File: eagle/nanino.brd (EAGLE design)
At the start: 68.6 x 53.3 mm, 19 parts, among them IC1 ATMEGA328P-20, Q1 16MHz

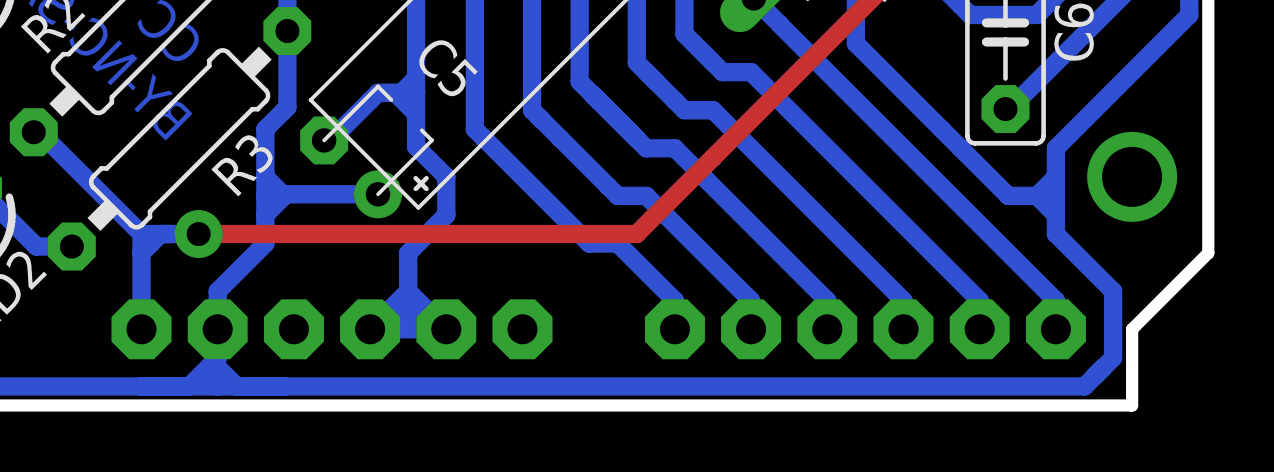
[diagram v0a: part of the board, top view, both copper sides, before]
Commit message: Power was connected to 3.3V Pin, not to 5V
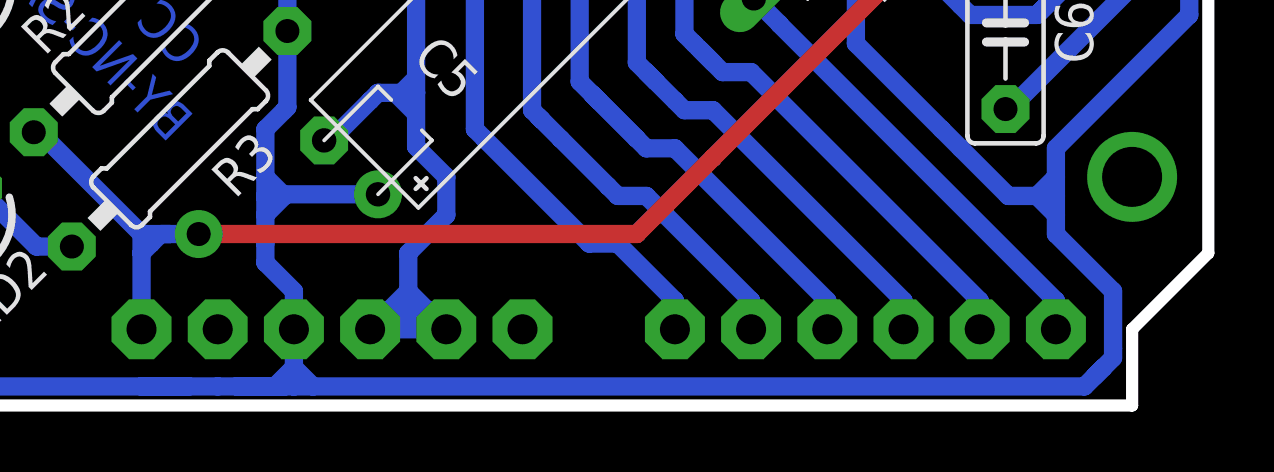
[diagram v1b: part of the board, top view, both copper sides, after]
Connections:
- net VCC: now also PWR_.3; no longer PWR_.2
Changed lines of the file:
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@@
 <layers>
 <layer number="1" name="Top" color="4" fill="1" visible="yes" active="yes"/>
-<layer number="16" name="Bottom" color="1" fill="1" visible="no" active="yes"/>
+<layer number="16" name="Bottom" color="1" fill="1" visible="yes" active="yes"/>
 <layer number="17" name="Pads" color="2" fill="1" visible="yes" active="yes"/>
 <layer number="18" name="Vias" color="2" fill="1" visible="yes" active="yes"/>
@@
 <contactref element="R2" pad="2"/>
 <contactref element="FTDI_" pad="3"/>
-<contactref element="PWR_" pad="2"/>
+<contactref element="PWR_" pad="3"/>
 <contactref element="IC1" pad="7"/>
 <contactref element="IC1" pad="20"/>
@@
 <wire x1="33.02" y1="0.635" x2="25.7175" y2="0.635" width="0.6096" layer="16"/>
 <wire x1="37.465" y1="0.635" x2="37.7825" y2="0.635" width="0.6096" layer="16"/>
-<wire x1="37.7825" y1="0.635" x2="64.4525" y2="0.635" width="0.6096" layer="16"/>
+<wire x1="37.7825" y1="0.635" x2="38.1" y2="0.635" width="0.6096" layer="16"/>
+<wire x1="38.1" y1="0.635" x2="38.735" y2="0.635" width="0.6096" layer="16"/>
+<wire x1="38.735" y1="0.635" x2="64.4525" y2="0.635" width="0.6096" layer="16"/>
 <wire x1="64.4525" y1="0.635" x2="65.0875" y2="1.27" width="0.6096" layer="16"/>
 <wire x1="24.4475" y1="0.9525" x2="24.765" y2="0.635" width="0.6096" layer="16"/>
 <wire x1="24.765" y1="0.635" x2="25.7175" y2="0.635" width="0.6096" layer="16"/>
-<wire x1="35.56" y1="2.54" x2="35.56" y2="1.5875" width="0.6096" layer="16"/>
-<wire x1="35.56" y1="1.5875" x2="34.6075" y2="0.635" width="0.6096" layer="16"/>
 <wire x1="34.6075" y1="0.635" x2="33.02" y2="0.635" width="0.6096" layer="16"/>
 <wire x1="33.02" y1="0.635" x2="35.56" y2="0.635" width="0.6096" layer="16"/>
 <wire x1="35.56" y1="0.635" x2="36.195" y2="0.635" width="0.6096" layer="16"/>
-<wire x1="36.195" y1="0.635" x2="37.7825" y2="0.635" width="0.6096" layer="16"/>
-<wire x1="37.7825" y1="0.635" x2="36.195" y2="0.635" width="0.6096" layer="16"/>
-<wire x1="36.195" y1="0.635" x2="35.56" y2="1.27" width="0.6096" layer="16"/>
-<wire x1="35.56" y1="1.27" x2="35.56" y2="0.635" width="0.6096" layer="16"/>
+<wire x1="36.195" y1="0.635" x2="37.465" y2="0.635" width="0.6096" layer="16"/>
+<wire x1="37.465" y1="0.635" x2="37.7825" y2="0.635" width="0.6096" layer="16"/>
+<wire x1="37.7825" y1="0.635" x2="37.465" y2="0.635" width="0.6096" layer="16"/>
+<wire x1="37.465" y1="0.635" x2="36.195" y2="0.635" width="0.6096" layer="16"/>
 <wire x1="38.4175" y1="15.5575" x2="40.005" y2="15.5575" width="0.6096" layer="16"/>
 <wire x1="40.005" y1="15.5575" x2="40.376971875" y2="15.929471875" width="0.6096" layer="16"/>
@@
 <wire x1="37.1475" y1="7.62" x2="37.1475" y2="6.985" width="0.6096" layer="16"/>
 <wire x1="37.1475" y1="6.985" x2="37.1475" y2="6.933471875" width="0.6096" layer="16"/>
-<wire x1="35.56" y1="2.54" x2="35.56" y2="3.81" width="0.6096" layer="16"/>
-<wire x1="35.56" y1="3.81" x2="37.1475" y2="5.3975" width="0.6096" layer="16"/>
 <wire x1="37.1475" y1="5.3975" x2="37.1475" y2="6.35" width="0.6096" layer="16"/>
 <wire x1="37.1475" y1="6.35" x2="37.1475" y2="6.933471875" width="0.6096" layer="16"/>
@@
 <wire x1="63.5" y1="7.62" x2="62.865" y2="6.985" width="0.6096" layer="16"/>
 <wire x1="62.865" y1="6.985" x2="63.5" y2="6.35" width="0.6096" layer="16"/>
+<wire x1="37.1475" y1="5.3975" x2="37.1475" y2="4.7625" width="0.6096" layer="16"/>
+<wire x1="37.1475" y1="4.7625" x2="38.1" y2="3.81" width="0.6096" layer="16"/>
+<wire x1="38.1" y1="3.81" x2="38.1" y2="2.54" width="0.6096" layer="16"/>
+<wire x1="38.1" y1="2.54" x2="38.1" y2="1.27" width="0.6096" layer="16"/>
+<wire x1="38.1" y1="1.27" x2="38.1" y2="0.635" width="0.6096" layer="16"/>
+<wire x1="38.1" y1="1.27" x2="37.465" y2="0.635" width="0.6096" layer="16"/>
+<wire x1="38.1" y1="1.27" x2="38.735" y2="0.635" width="0.6096" layer="16"/>
 </signal>
 <signal name="N$34">
@@
 </signal>
 </signals>
-<errors>
-</errors>
 </board>
 </drawing>

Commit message: 5V power was connected to 3.3V Pin
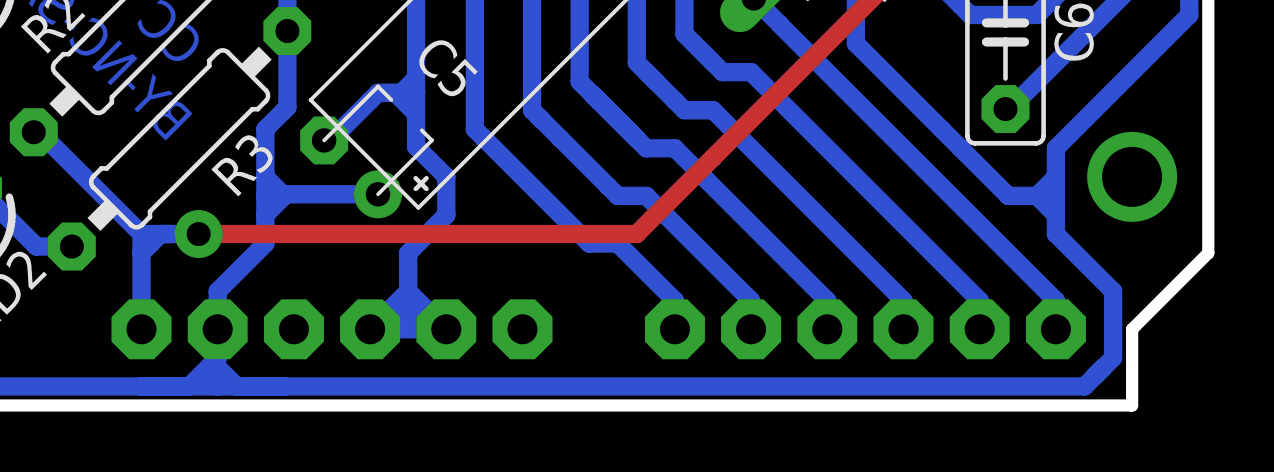
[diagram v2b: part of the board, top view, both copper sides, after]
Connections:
- net VCC: now also PWR_.2; no longer PWR_.3
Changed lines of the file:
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@@
 <layers>
 <layer number="1" name="Top" color="4" fill="1" visible="yes" active="yes"/>
-<layer number="16" name="Bottom" color="1" fill="1" visible="yes" active="yes"/>
+<layer number="16" name="Bottom" color="1" fill="1" visible="no" active="yes"/>
 <layer number="17" name="Pads" color="2" fill="1" visible="yes" active="yes"/>
 <layer number="18" name="Vias" color="2" fill="1" visible="yes" active="yes"/>
@@
 <contactref element="R2" pad="2"/>
 <contactref element="FTDI_" pad="3"/>
-<contactref element="PWR_" pad="3"/>
+<contactref element="PWR_" pad="2"/>
 <contactref element="IC1" pad="7"/>
 <contactref element="IC1" pad="20"/>
@@
 <wire x1="33.02" y1="0.635" x2="25.7175" y2="0.635" width="0.6096" layer="16"/>
 <wire x1="37.465" y1="0.635" x2="37.7825" y2="0.635" width="0.6096" layer="16"/>
-<wire x1="37.7825" y1="0.635" x2="38.1" y2="0.635" width="0.6096" layer="16"/>
-<wire x1="38.1" y1="0.635" x2="38.735" y2="0.635" width="0.6096" layer="16"/>
-<wire x1="38.735" y1="0.635" x2="64.4525" y2="0.635" width="0.6096" layer="16"/>
+<wire x1="37.7825" y1="0.635" x2="64.4525" y2="0.635" width="0.6096" layer="16"/>
 <wire x1="64.4525" y1="0.635" x2="65.0875" y2="1.27" width="0.6096" layer="16"/>
 <wire x1="24.4475" y1="0.9525" x2="24.765" y2="0.635" width="0.6096" layer="16"/>
 <wire x1="24.765" y1="0.635" x2="25.7175" y2="0.635" width="0.6096" layer="16"/>
+<wire x1="35.56" y1="2.54" x2="35.56" y2="1.5875" width="0.6096" layer="16"/>
+<wire x1="35.56" y1="1.5875" x2="34.6075" y2="0.635" width="0.6096" layer="16"/>
 <wire x1="34.6075" y1="0.635" x2="33.02" y2="0.635" width="0.6096" layer="16"/>
 <wire x1="33.02" y1="0.635" x2="35.56" y2="0.635" width="0.6096" layer="16"/>
 <wire x1="35.56" y1="0.635" x2="36.195" y2="0.635" width="0.6096" layer="16"/>
-<wire x1="36.195" y1="0.635" x2="37.465" y2="0.635" width="0.6096" layer="16"/>
-<wire x1="37.465" y1="0.635" x2="37.7825" y2="0.635" width="0.6096" layer="16"/>
-<wire x1="37.7825" y1="0.635" x2="37.465" y2="0.635" width="0.6096" layer="16"/>
-<wire x1="37.465" y1="0.635" x2="36.195" y2="0.635" width="0.6096" layer="16"/>
+<wire x1="36.195" y1="0.635" x2="37.7825" y2="0.635" width="0.6096" layer="16"/>
+<wire x1="37.7825" y1="0.635" x2="36.195" y2="0.635" width="0.6096" layer="16"/>
+<wire x1="36.195" y1="0.635" x2="35.56" y2="1.27" width="0.6096" layer="16"/>
+<wire x1="35.56" y1="1.27" x2="35.56" y2="0.635" width="0.6096" layer="16"/>
 <wire x1="38.4175" y1="15.5575" x2="40.005" y2="15.5575" width="0.6096" layer="16"/>
 <wire x1="40.005" y1="15.5575" x2="40.376971875" y2="15.929471875" width="0.6096" layer="16"/>
@@
 <wire x1="37.1475" y1="7.62" x2="37.1475" y2="6.985" width="0.6096" layer="16"/>
 <wire x1="37.1475" y1="6.985" x2="37.1475" y2="6.933471875" width="0.6096" layer="16"/>
+<wire x1="35.56" y1="2.54" x2="35.56" y2="3.81" width="0.6096" layer="16"/>
+<wire x1="35.56" y1="3.81" x2="37.1475" y2="5.3975" width="0.6096" layer="16"/>
 <wire x1="37.1475" y1="5.3975" x2="37.1475" y2="6.35" width="0.6096" layer="16"/>
 <wire x1="37.1475" y1="6.35" x2="37.1475" y2="6.933471875" width="0.6096" layer="16"/>
@@
 <wire x1="63.5" y1="7.62" x2="62.865" y2="6.985" width="0.6096" layer="16"/>
 <wire x1="62.865" y1="6.985" x2="63.5" y2="6.35" width="0.6096" layer="16"/>
-<wire x1="37.1475" y1="5.3975" x2="37.1475" y2="4.7625" width="0.6096" layer="16"/>
-<wire x1="37.1475" y1="4.7625" x2="38.1" y2="3.81" width="0.6096" layer="16"/>
-<wire x1="38.1" y1="3.81" x2="38.1" y2="2.54" width="0.6096" layer="16"/>
-<wire x1="38.1" y1="2.54" x2="38.1" y2="1.27" width="0.6096" layer="16"/>
-<wire x1="38.1" y1="1.27" x2="38.1" y2="0.635" width="0.6096" layer="16"/>
-<wire x1="38.1" y1="1.27" x2="37.465" y2="0.635" width="0.6096" layer="16"/>
-<wire x1="38.1" y1="1.27" x2="38.735" y2="0.635" width="0.6096" layer="16"/>
 </signal>
 <signal name="N$34">
@@
 </signal>
 </signals>
+<errors>
+</errors>
 </board>
 </drawing>
